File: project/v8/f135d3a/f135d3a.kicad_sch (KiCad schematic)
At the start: 1 part

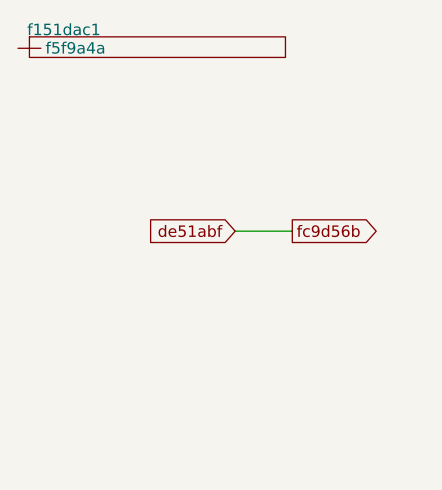
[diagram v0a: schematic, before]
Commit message: 14-add-leftright-to-choose-location-of-the-pins: now position of the pin is not tied to shape of the pin so I can put bidirectional pin also directional pin added to two.csv
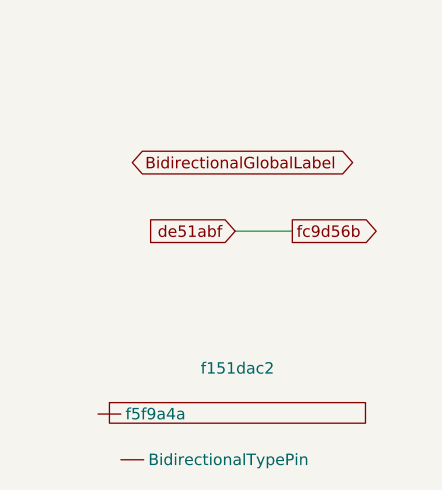
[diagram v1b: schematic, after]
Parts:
- removed f151dac1: ~, symbol e5ea7ba:a87e18d
- added f151dac2: ~, symbol e5ea7ba:a87e18d
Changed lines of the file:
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@@
+		)
+	)
+	(global_label "BidirectionalGlobalLabel"
+		(shape bidirectional)
+		(at 12.7 16.51 0)
+		(fields_autoplaced yes)
+		(effects
+			(font
+				(size 1.27 1.27)
+			)
+			(justify left)
+		)
+		(property "Intersheetrefs" "${INTERSHEET_REFS}"
+			(at 39.9585 16.51 0)
+			(effects
+				(font
+					(size 1.27 1.27)
+				)
+				(justify left)
+				(hide yes)
+			)
 		)
 	)
@@
 	)
 	(symbol
+		(lib_name "a87e18d_1")
 		(lib_id "e5ea7ba:a87e18d")
-		(at 0 0 0)
+		(at 8.89 40.64 0)
 		(unit 1)
 		(exclude_from_sim no)
@@
 		(on_board yes)
 		(dnp no)
-		(property "Reference" "f151dac1"
-			(at 1.016 1.016 0)
+		(fields_autoplaced yes)
+		(property "Reference" "f151dac2"
+			(at 24.384 39.37 0)
 			(effects
 				(font
@@
 					(size 1.27 1.27)
 				)
-				(justify left top)
 			)
 		)
 		(property "Value" "~"
-			(at 0 0 0)
+			(at 24.384 41.91 0)
 			(effects
 				(font
@@
 		)
 		(property "Footprint" ""
-			(at 0 0 0)
+			(at 8.89 40.64 0)
 			(effects
 				(font
@@
 		)
 		(property "Datasheet" ""
-			(at 0 0 0)
+			(at 8.89 40.64 0)
 			(effects
 				(font
@@
 		)
 		(property "Description" ""
-			(at 0 0 0)
+			(at 8.89 40.64 0)
 			(effects
 				(font
@@
 		(pin ""
 		)
+		(pin "1"
+		)
 		(instances
 			(project ""
 				(path "/97f17985-da40-43fd-b268-8c96b481a2af"
-					(reference "f151dac1")
+					(reference "f151dac2")
 					(unit 1)
 				)

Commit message: 29-support-multiple-instantantion-of-same-symbol: single symbol in page in project modified to support multiple instantion of same symbol
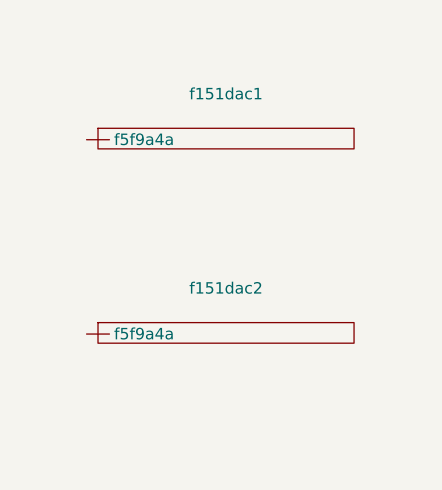
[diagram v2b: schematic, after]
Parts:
- added f151dac1: ~, symbol e5ea7ba:a87e18d
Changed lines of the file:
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@@
 	(generator_version "8.0")
 	(paper "User" 999 666)
-	(wire
-		(pts
-			(xy 24.13 24.13) (xy 30.48 24.13)
-		)
-		(stroke
-			(width 0)
-			(type default)
-		)
-	)
-	(global_label "BidirectionalGlobalLabel"
-		(shape bidirectional)
-		(at 12.7 16.51 0)
-		(fields_autoplaced yes)
-		(effects
-			(font
-				(size 1.27 1.27)
-			)
-			(justify left)
-		)
-		(property "Intersheetrefs" "${INTERSHEET_REFS}"
-			(at 39.9585 16.51 0)
-			(effects
-				(font
-					(size 1.27 1.27)
-				)
-				(justify left)
-				(hide yes)
-			)
-		)
-	)
-	(global_label "fc9d56b"
-		(shape output)
-		(at 30.48 24.13 0)
-		(fields_autoplaced yes)
-		(effects
-			(font
-				(size 1.27 1.27)
-			)
-			(justify left)
-		)
-		(property "Intersheetrefs" "${INTERSHEET_REFS}"
-			(at 41.206 24.13 0)
-			(effects
-				(font
-					(size 1.27 1.27)
-				)
-				(justify left)
-				(hide yes)
-			)
-		)
-	)
-	(global_label "de51abf"
-		(shape input)
-		(at 24.13 24.13 180)
-		(fields_autoplaced yes)
-		(effects
-			(font
-				(size 1.27 1.27)
-			)
-			(justify right)
-		)
-		(property "Intersheetrefs" "${INTERSHEET_REFS}"
-			(at 13.4645 24.13 0)
-			(effects
-				(font
-					(size 1.27 1.27)
-				)
-				(justify right)
-				(hide yes)
-			)
-		)
-	)
 	(symbol
-		(lib_name "a87e18d_1")
 		(lib_id "e5ea7ba:a87e18d")
-		(at 8.89 40.64 0)
+		(at 7.62 31.75 0)
 		(unit 1)
 		(exclude_from_sim no)
@@
 		(fields_autoplaced yes)
 		(property "Reference" "f151dac2"
-			(at 24.384 39.37 0)
+			(at 23.114 30.48 0)
 			(effects
 				(font
@@
 		)
 		(property "Value" "~"
-			(at 24.384 41.91 0)
+			(at 23.114 33.02 0)
 			(effects
 				(font
@@
 		)
 		(property "Footprint" ""
-			(at 8.89 40.64 0)
+			(at 7.62 31.75 0)
 			(effects
 				(font
@@
 		)
 		(property "Datasheet" ""
-			(at 8.89 40.64 0)
+			(at 7.62 31.75 0)
 			(effects
 				(font
@@
 		)
 		(property "Description" ""
-			(at 8.89 40.64 0)
+			(at 7.62 31.75 0)
 			(effects
 				(font
@@
 		(pin ""
 		)
-		(pin "1"
-		)
 		(instances
 			(project ""
@@
 					(unit 1)
 				)
+			)
+		)
+	)
+	(symbol
+		(lib_id "e5ea7ba:a87e18d")
+		(at 7.62 10.16 0)
+		(unit 1)
+		(exclude_from_sim no)
+		(in_bom yes)
+		(on_board yes)
+		(dnp no)
+		(fields_autoplaced yes)
+		(property "Reference" "f151dac1"
+			(at 23.114 8.89 0)
+			(effects
+				(font
+					(face "Cascadia Mono")
+					(size 1.27 1.27)
+				)
+			)
+		)
+		(property "Value" "~"
+			(at 23.114 11.43 0)
+			(effects
+				(font
+					(size 1.27 1.27)
+				)
+			)
+		)
+		(property "Footprint" ""
+			(at 7.62 10.16 0)
+			(effects
+				(font
+					(size 1.27 1.27)
+				)
+				(hide yes)
+			)
+		)
+		(property "Datasheet" ""
+			(at 7.62 10.16 0)
+			(effects
+				(font
+					(size 1.27 1.27)
+				)
+				(hide yes)
+			)
+		)
+		(property "Description" ""
+			(at 7.62 10.16 0)
+			(effects
+				(font
+					(size 1.27 1.27)
+				)
+				(hide yes)
+			)
+		)
+		(pin ""
+		)
+		(instances
+			(project ""
+				(path "/97f17985-da40-43fd-b268-8c96b481a2af"
+					(reference "f151dac1")
+					(unit 1)
+				)
